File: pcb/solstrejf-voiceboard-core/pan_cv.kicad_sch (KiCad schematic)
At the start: 0 parts

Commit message: Inital draft of the voice board power supplys and core.
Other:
- title: (none) -> Pan Control Voltage Summing Amplifier
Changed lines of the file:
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@@
 	(generator_version "8.0")
 	(paper "A4")
+	(title_block
+		(title "Pan Control Voltage Summing Amplifier")
+		(date "2024-08-24")
+		(rev "1.0")
+	)
 )

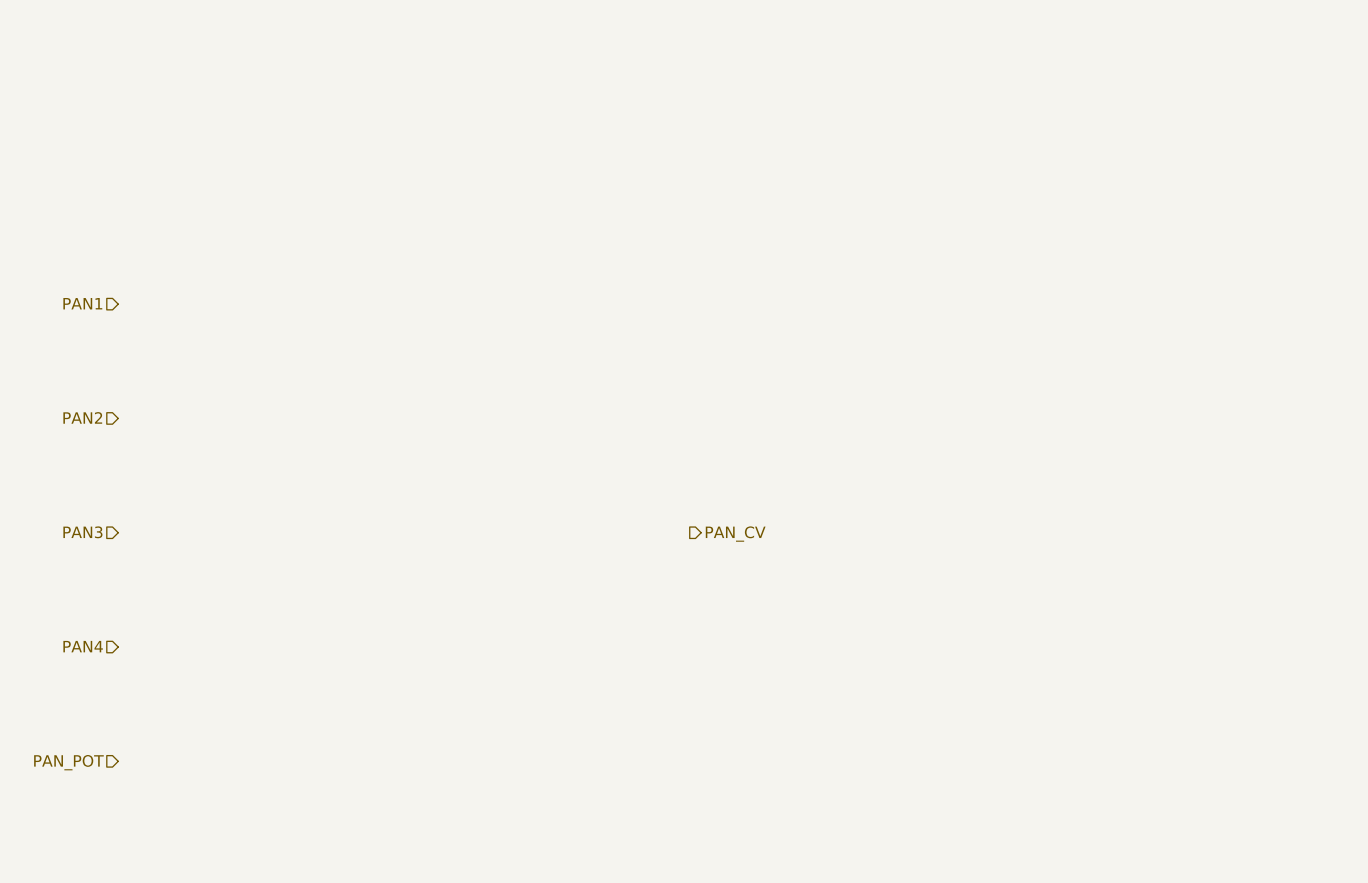
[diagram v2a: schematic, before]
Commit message: created schematic for CV circuits: PAN, VCA, and FREQ. Created a new symbol for the ONESHOT envelope generator
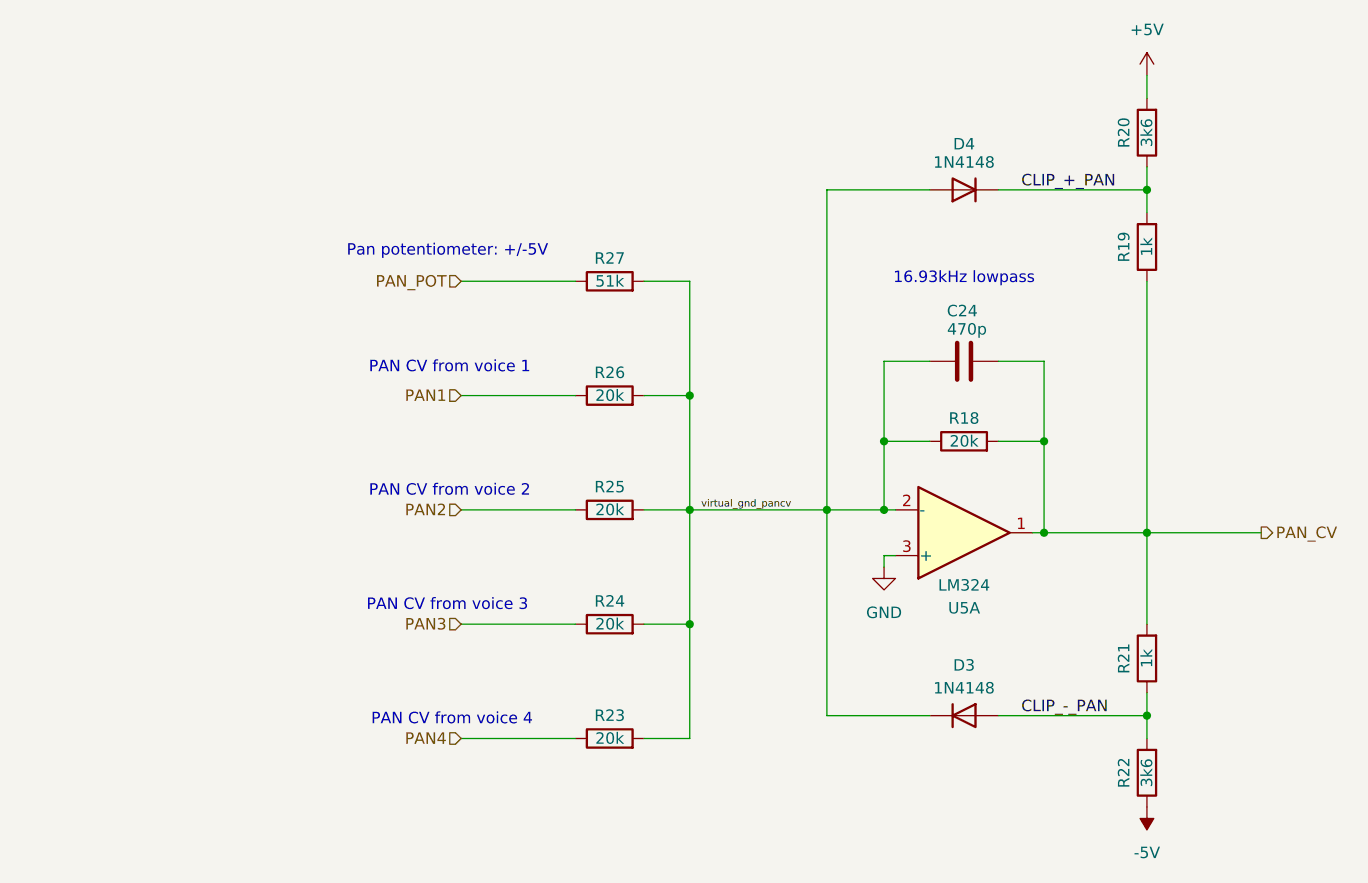
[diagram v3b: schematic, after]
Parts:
- added C24: 470p, Capacitor_THT:C_Disc_D5.0mm_W2.5mm_P5.00mm, symbol Device:C
- added D3, D4: 1N4148, Diode_THT:D_DO-35_SOD27_P7.62mm_Horizontal, symbol Diode:1N4148
- added R18, R23, R24, R25, R26: 20k, Resistor_THT:R_Axial_DIN0207_L6.3mm_D2.5mm_P10.16mm_Horizontal, symbol Device:R
- added R19, R21: 1k, Resistor_THT:R_Axial_DIN0207_L6.3mm_D2.5mm_P10.16mm_Horizontal, symbol Device:R
- added R20, R22: 3k6, Resistor_THT:R_Axial_DIN0207_L6.3mm_D2.5mm_P10.16mm_Horizontal, symbol Device:R
- added R27: 51k, Resistor_THT:R_Axial_DIN0207_L6.3mm_D2.5mm_P10.16mm_Horizontal, symbol Device:R
- added U5: LM324, Package_DIP:DIP-14_W7.62mm, symbol Amplifier_Operational:LM324
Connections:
- net PAN1: now also R26.1
- net PAN2: now also R25.1
- net PAN3: now also R24.1
- net PAN4: now also R23.1
- net PAN_CV: now also C24.2, R18.2, R19.1, R21.2, U5.1
- net PAN_POT: now also R27.1
- new net +5V: R20.2
- new net -5V: R22.1
- new net CLIP_+_PAN: D4.1 (K), R19.2, R20.1
- new net CLIP_-_PAN: D3.2 (A), R21.1, R22.2
- new net GND: U5.3 (+)
- new net virtual_gnd_pancv: C24.1, D3.1 (K), D4.2 (A), R18.1, R23.2, R24.2, R25.2, R26.2, R27.2, U5.2 (-)
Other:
- note added: "16.93kHz lowpass"
- note added: "PAN CV from voice 1"
- note added: "PAN CV from voice 2"
- note added: "PAN CV from voice 3"
- note added: "PAN CV from voice 4"
- note added: "Pan potentiometer: +/-5V"
